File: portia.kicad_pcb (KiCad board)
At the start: 2 copper layers, 56.2 x 31 mm, 17 parts, among them J1 VCC, J2 Conn_01x08, J3 Conn_01x08, J4 Conn_02x08_Counter_Clockwise, U1 LM1117-3.3, U4 ESP32-WROOM

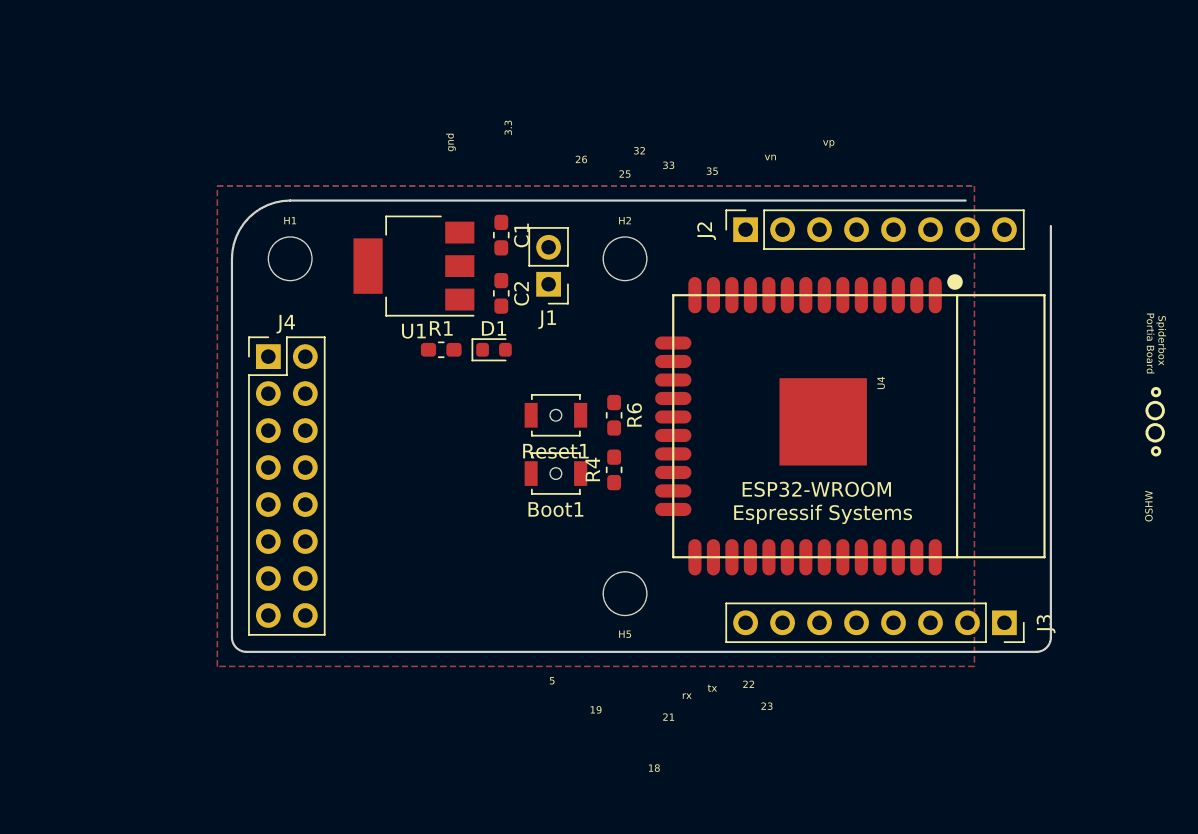
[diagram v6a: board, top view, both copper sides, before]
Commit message: update schematic
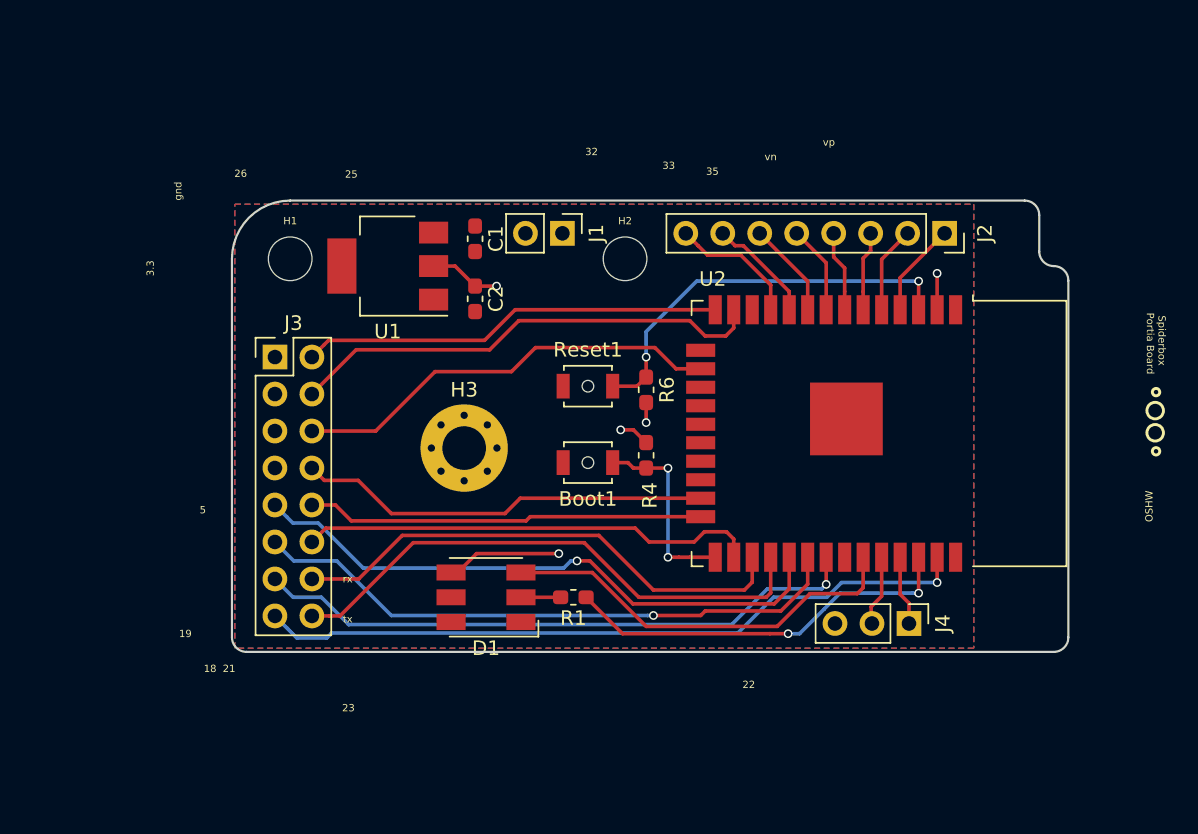
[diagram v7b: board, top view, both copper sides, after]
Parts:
- removed H5: MountingHole, sb_designed_footprints:MountingHole_3mm
- removed U4: ESP32-WROOM, ESP32-footprints-Lib:ESP32-WROOM
- added H3: MountingHole_Pad, MountingHole:MountingHole_3mm_Pad_Via, F.Cu at (172.0, 120.3)
- added U2: ESP32-WROOM-32, RF_Module:ESP32-WROOM-32, F.Cu at (197.5, 119.3)
- D1: value LED_Small -> LED_ARGB; footprint LED_SMD:LED_0603_1608Metric -> LED_SMD:LED_RGB_5050-6
- J3: value Conn_01x08 -> Conn_02x08_Odd_Even; footprint Connector_PinSocket_2.54mm:PinSocket_1x08_P2.54mm_Vertical -> Connector_PinHeader_2.54mm:PinHeader_2x08_P2.54mm_Vertical
- J4: value Conn_02x08_Counter_Clockwise -> Conn_01x03; footprint Connector_PinHeader_2.54mm:PinHeader_2x08_P2.54mm_Vertical -> Connector_PinHeader_2.54mm:PinHeader_1x03_P2.54mm_Vertical
- moved J3 53.3 mm to (159.0, 114.0), turned to 0 degrees
- moved J4 47.7 mm to (202.5, 132.3), turned to 270 degrees
- moved R1 19.3 mm to (179.5, 130.5), turned to 180 degrees
- moved D1 17.0 mm to (173.5, 130.5), turned to 180 degrees
- moved J2 13.7 mm to (205.0, 105.5), turned to 270 degrees
- moved J1 3.63 mm to (178.7, 105.5), turned to 270 degrees
- moved Reset1 2.97 mm to (180.5, 116.0), turned to 0 degrees
- moved R6 2.81 mm to (184.5, 116.3)
- moved R4 2.42 mm to (184.5, 120.8)
- moved Boot1 2.32 mm to (180.5, 121.3)
- moved C2 1.84 mm to (172.7, 110.0)
- moved C1 1.82 mm to (172.7, 105.9)
- moved U1 1.80 mm to (166.7, 107.8)
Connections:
- D1 pad 1: Net-(D1-Pad1) -> +3V3
- D1 pad 2: +3V3 -> Net-(D1-Pad2)
- J2 pad 1: Net-(J2-Pad1) -> /vp
- J2 pad 2: Net-(J2-Pad2) -> /vn
- J3 pad 1: Net-(J3-Pad1) -> +3V3
- J3 pad 2: Net-(J3-Pad2) -> /miso
- J3 pad 3: GND -> +3V3
- J3 pad 4: GND -> /sck
- J3 pad 5: Net-(J3-Pad5) -> GND
- J3 pad 6: Net-(J3-Pad6) -> /mosi
- J3 pad 8: Net-(J3-Pad8) -> /cs
- J4 pad 1: /io5_cs -> Net-(J4-Pad1)
- J4 pad 2: /io18_sck -> Net-(J4-Pad2)
- J4 pad 3: /io19_miso -> GND
- R1 pad 1: GND -> Net-(R1-Pad1)
- R1 pad 2: Net-(D1-Pad1) -> Net-(D1-Pad2)
- R4 pad 1: +3V3 -> Net-(Boot1-Pad1)
- R4 pad 2: Net-(Boot1-Pad1) -> +3V3
- Reset1 pad 1: Net-(R6-Pad1) -> GND
- Reset1 pad 2: GND -> Net-(R6-Pad1)
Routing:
- net /io23_mosi: track 0.00 -> 49.4 mm, vias 0 -> 1
- net /io19_miso: track 0.00 -> 42.2 mm, vias 0 -> 1
- net /io18_sck: track 0.00 -> 41.4 mm, vias 0 -> 1
- net /io5_cs: track 0.00 -> 41.2 mm, vias 0 -> 1
- net /tx: track 0.00 -> 37.7 mm
- net /rx: track 0.00 -> 35.7 mm
- net /sck: track 0.00 -> 33.0 mm
- net /qhd: track 0.00 -> 31.5 mm
- net /mosi: track 0.00 -> 29.7 mm
- net /miso: track 0.00 -> 29.1 mm
- net /cs: track 0.00 -> 28.4 mm
- net Net-(D1-Pad3): track 0.00 -> 28.2 mm
- net Net-(R6-Pad1): track 0.00 -> 27.8 mm, vias 0 -> 2
- net Net-(R1-Pad1): track 0.00 -> 27.5 mm, vias 0 -> 2
- net /qwp: track 0.00 -> 27.3 mm
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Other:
- board size 56.2 x 31 mm -> 57.4 x 31 mm

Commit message: update pcb
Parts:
- moved R1 0.75 mm to (179.2, 129.8)
- moved J1 0.10 mm to (178.7, 105.4)
- renumbered Boot1 to Boot, Reset1 to Reset
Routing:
- net Net-(D1-Pad4): track 7.94 -> 37.4 mm, vias 1 -> 2
- net VCC: track 0.00 -> 7.23 mm
- net +3V3: track 11.0 -> 16.6 mm, vias 4 -> 5
- net Net-(R1-Pad1): track 27.5 -> 28.1 mm
- net /sck: vias 0 -> 2
- net /mosi: vias 0 -> 2
- net /miso: vias 0 -> 2
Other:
- net class power removed
- board text added: "12"
- board text added: "13"
- board text added: "14"
- board text added: "15"
- board text added: "2"
- board text added: "4"
- board text removed: "22"
- board text removed: "5"
